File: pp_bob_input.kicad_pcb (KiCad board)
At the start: 2 copper layers, 98.8 x 72.1 mm, 38 parts, among them P4 13X2, U1 74LVC245, U2 74LVC245, U3 74LS541

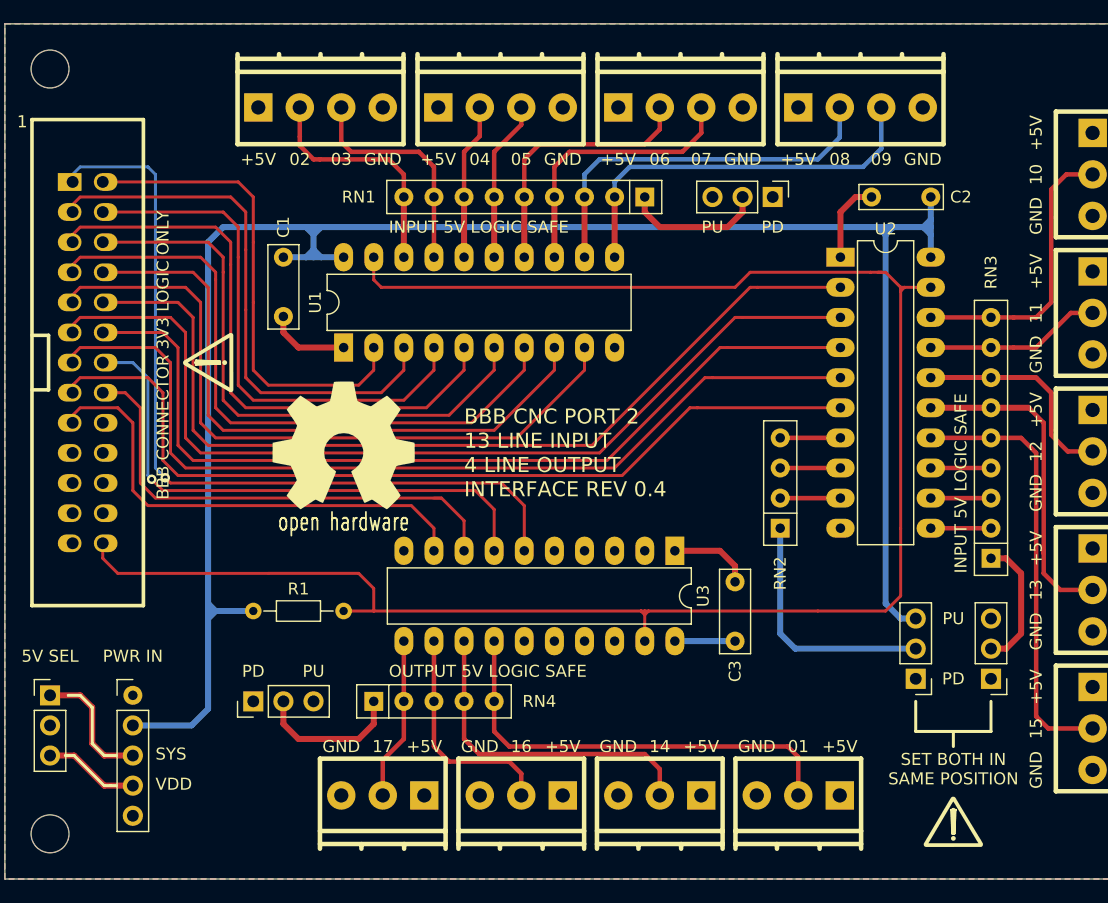
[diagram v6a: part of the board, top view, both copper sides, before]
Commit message: Move DB_02 to DB_09 to front & DB_01,14,16,17 to rear.
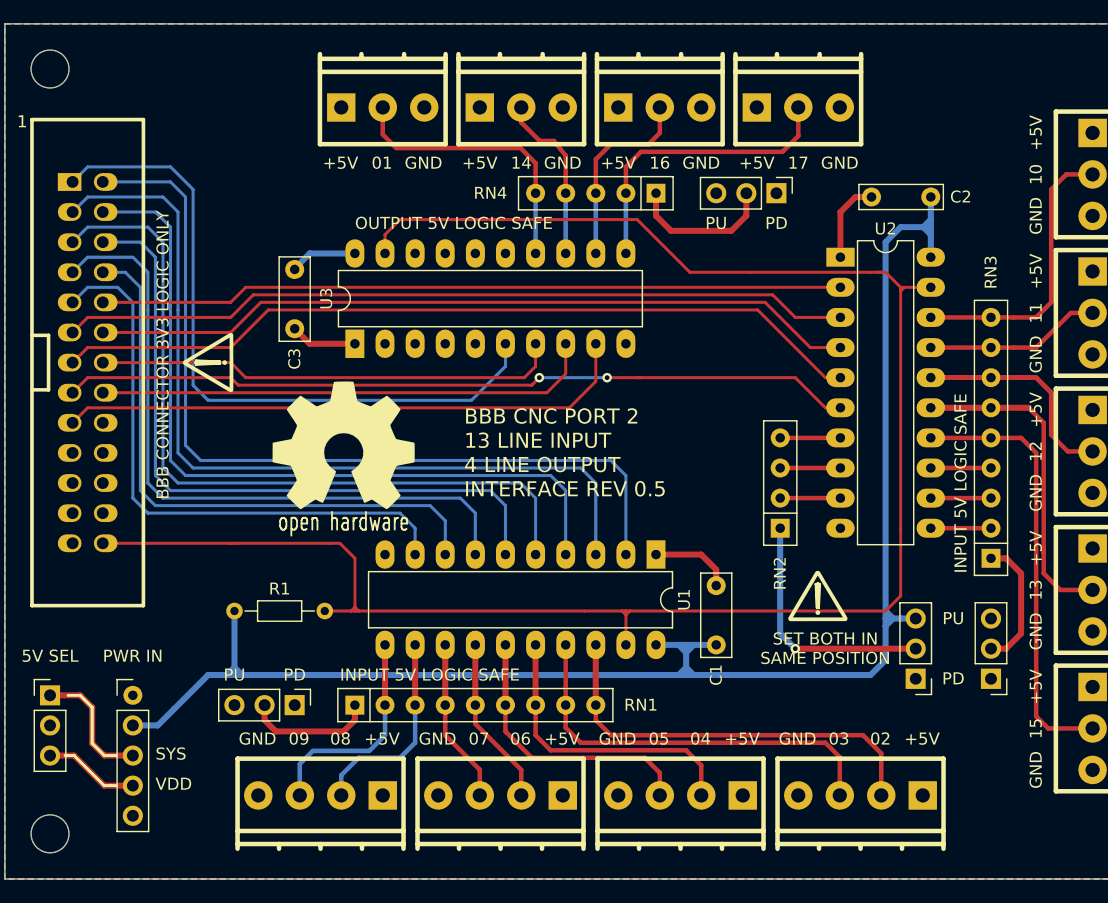
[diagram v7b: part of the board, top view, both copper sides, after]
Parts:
- moved J_IN_1 74.9 mm to (97.6, 91.2), turned to 0 degrees
- moved J_IN_4 74.9 mm to (52.0, 91.2), turned to 0 degrees
- moved J_OUT_5 69.0 mm to (57.3, 31.8), turned to 180 degrees
- moved J_OUT_8 69.0 mm to (92.3, 31.8), turned to 180 degrees
- moved SEL_4 61.5 mm to (90.5, 39.7), turned to 270 degrees
- moved J_IN_2 61.3 mm to (82.4, 91.2), turned to 0 degrees
- moved J_IN_3 61.3 mm to (67.2, 91.2), turned to 0 degrees
- moved J_OUT_6 60.6 mm to (69.0, 31.8), turned to 180 degrees
- moved J_OUT_7 60.6 mm to (80.6, 31.8), turned to 180 degrees
- moved SEL_1 58.8 mm to (49.8, 82.9)
- moved RN1 49.3 mm to (54.9, 82.9), turned to 0 degrees
- moved RN4 49.0 mm to (80.3, 39.7), turned to 180 degrees
- moved C1 49.0 mm to (85.4, 77.8), turned to 90 degrees
- moved C3 45.5 mm to (49.8, 51.1)
- moved U3 32.1 mm to (54.9, 52.4), turned to 90 degrees
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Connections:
- C3 pad 1: +5V -> GND
- C3 pad 2: GND -> +5V
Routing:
- net +3V3: track 168.4 -> 135.3 mm
- net DB_02: track 41.6 -> 73.3 mm
- net DB_03: track 47.2 -> 73.2 mm
- net DB_04: track 45.9 -> 65.7 mm
- net DB_10: track 79.0 -> 62.8 mm
- net /IN-02: track 20.6 -> 35.8 mm
- net /IN-03: track 19.2 -> 34.4 mm
- net /IN-09: track 33.5 -> 18.5 mm
- net /IN-08: track 32.3 -> 17.3 mm
- net DB_05: track 50.9 -> 65.0 mm
- net /OUT-01: track 37.4 -> 23.8 mm
- net DB_11: track 80.3 -> 67.5 mm
- net /OUT-14: track 28.0 -> 15.8 mm
- net /IN-04: track 13.2 -> 25.2 mm
- net /OUT-17: track 13.8 -> 25.3 mm
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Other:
- board text added: "BBB CNC PORT 2 13 LINE INPUT 4 LINE OUTPUT INTERFACE REV 0.5"
- board text removed: "BBB CNC PORT 2 13 LINE INPUT 4 LINE OUTPUT INTERFACE REV 0.4"

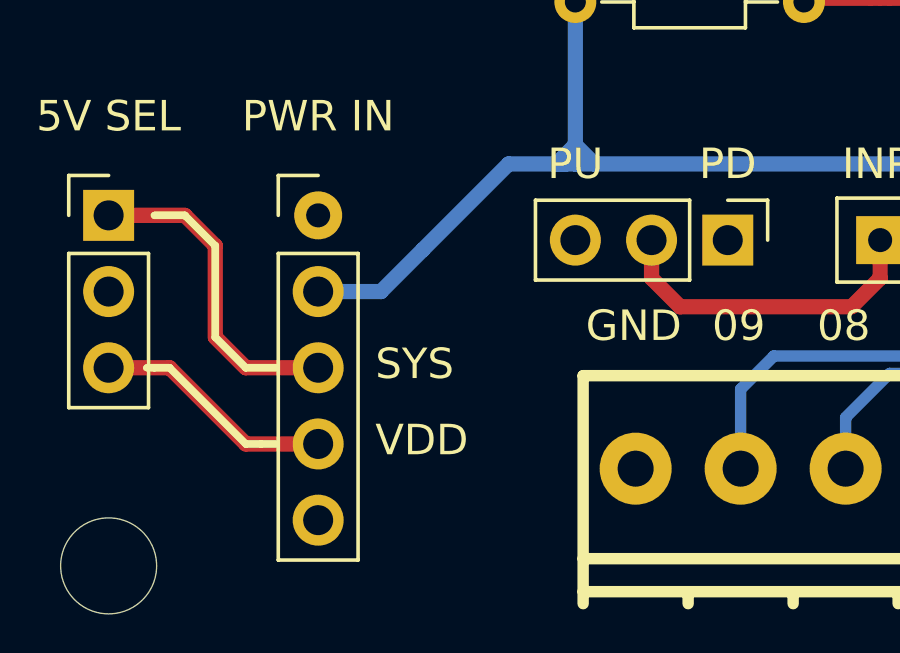
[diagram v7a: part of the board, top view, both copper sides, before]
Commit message: Fix silkscreen
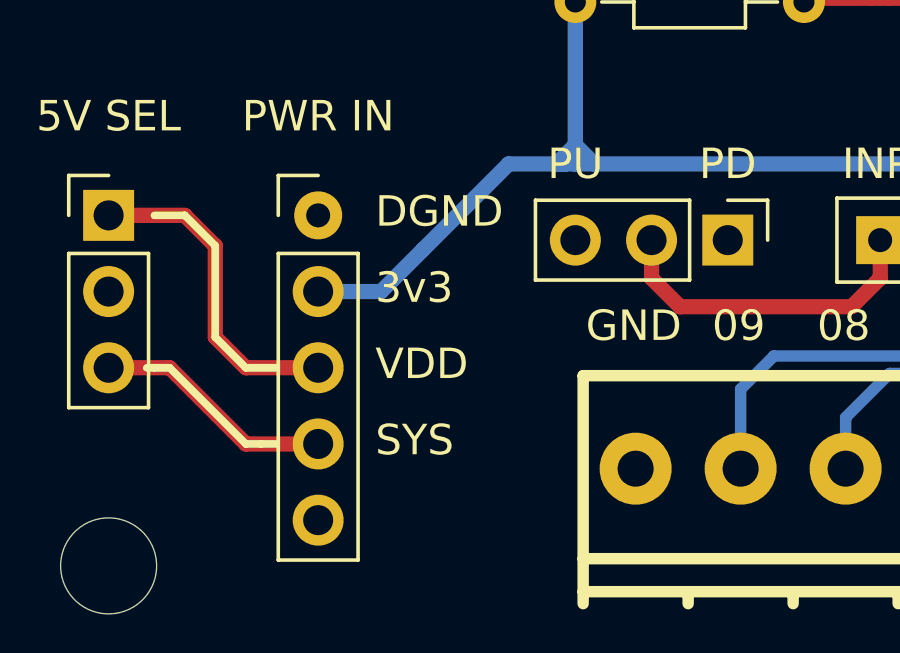
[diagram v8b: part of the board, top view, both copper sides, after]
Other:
- board text added: "3v3"
- board text added: "DGND"
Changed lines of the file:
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@@
-(kicad_pcb (version 4) (host pcbnew 4.0.6-e0-6349~53~ubuntu16.04.1)
+(kicad_pcb (version 4) (host pcbnew 4.0.7-e2-6376~58~ubuntu16.04.1)
   (general
     (links 129)
     (no_connects 0)
-    (area 25.387299 25.387299 124.218701 97.548701)
+    (area 25.248095 24.035 124.706 99.001)
     (thickness 1.6)
-    (drawings 78)
+    (drawings 80)
     (tracks 372)
     (zones 0)
@@
   (page A4)
   (layers
-    (0 F.Cu signal)
-    (31 B.Cu signal)
+    (0 F.Cu signal hide)
+    (31 B.Cu signal hide)
     (33 F.Adhes user)
     (35 F.Paste user)
@@
   )
   (setup
-    (last_trace_width 0.254)
+    (last_trace_width 0.25)
     (user_trace_width 0.0254)
     (user_trace_width 0.254)
@@
     )
   )
+  (gr_text DGND (at 38.1 81.915) (layer F.SilkS)
+    (effects (font (size 1.016 1.016) (thickness 0.2032)) (justify left))
+  )
+  (gr_text 3v3 (at 38.1 84.455) (layer F.SilkS)
+    (effects (font (size 1.016 1.016) (thickness 0.2032)) (justify left))
+  )
   (gr_text PD (at 90.4875 42.2275) (layer F.SilkS)
     (effects (font (size 1.016 1.016) (thickness 0.2032)))
@@
     (effects (font (size 1.016 1.016) (thickness 0.2032)))
   )
-  (gr_text VDD (at 38.1 89.535) (layer F.SilkS)
+  (gr_text SYS (at 38.1 89.535) (layer F.SilkS)
     (effects (font (size 1.016 1.016) (thickness 0.2032)) (justify left))
   )
-  (gr_text SYS (at 38.1 86.995) (layer F.SilkS)
+  (gr_text VDD (at 38.1 86.995) (layer F.SilkS)
     (effects (font (size 1.016 1.016) (thickness 0.2032)) (justify left))
   )
